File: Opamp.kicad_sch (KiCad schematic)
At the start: 7 parts, among them Q2 NPN, Q3 NPN, U1 ADA4522-2ARMZ-R7, U2 MCP4232-503E/UN

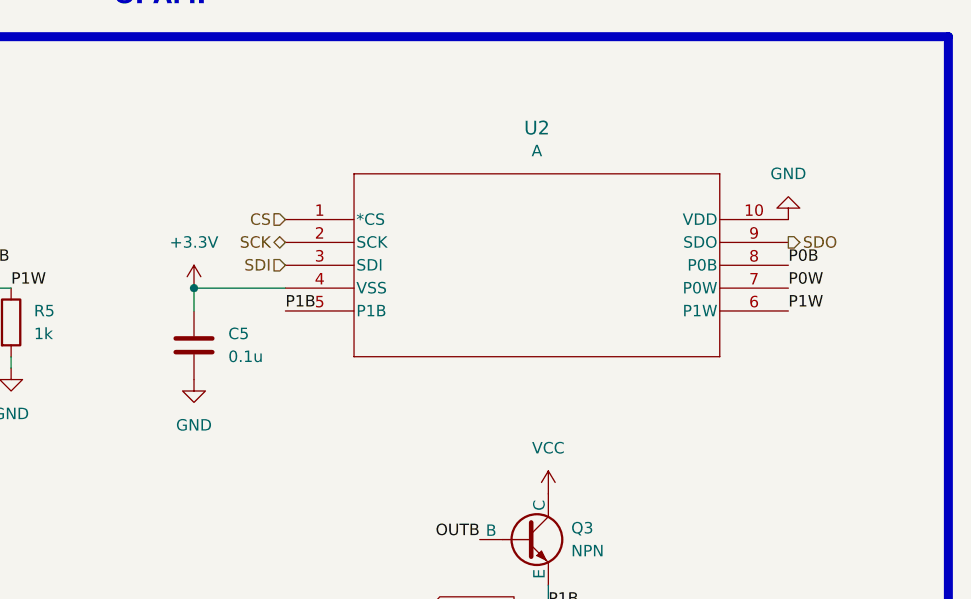
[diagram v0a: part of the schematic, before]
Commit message: version 2 with 0.8mm thickness
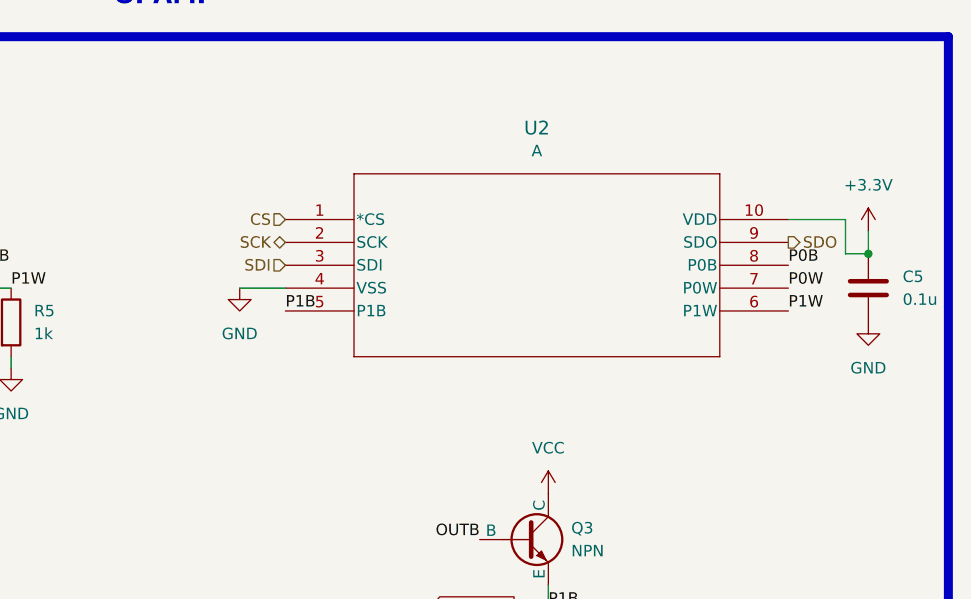
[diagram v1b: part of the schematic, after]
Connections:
- net +3.3V: now also U2.10 (VDD); no longer U2.4 (VSS)
- net GND: now also U2.4 (VSS); no longer U2.10 (VDD)
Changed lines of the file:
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@@
 (kicad_sch (version 20230121) (generator eeschema)
   (paper "A4")
-  (junction (at 152.4 88.9) (diameter 0) (color 0 0 0 0)
+  (junction (at 227.33 85.09) (diameter 0) (color 0 0 0 0)
   )
   (wire (pts (xy 187.96 124.46) (xy 191.77 124.46))
@@
     (stroke (width 0) (type default))
   )
-  (wire (pts (xy 152.4 88.9) (xy 162.56 88.9))
+  (wire (pts (xy 157.48 88.9) (xy 162.56 88.9))
+    (stroke (width 0) (type default))
+  )
+  (wire (pts (xy 224.79 81.28) (xy 224.79 85.09))
+    (stroke (width 0) (type default))
+  )
+  (wire (pts (xy 224.79 85.09) (xy 227.33 85.09))
+    (stroke (width 0) (type default))
+  )
+  (wire (pts (xy 227.33 85.09) (xy 227.33 82.55))
     (stroke (width 0) (type default))
   )
@@
     (stroke (width 0) (type default))
   )
-  (wire (pts (xy 152.4 91.44) (xy 152.4 88.9))
+  (wire (pts (xy 218.44 81.28) (xy 224.79 81.28))
     (stroke (width 0) (type default))
   )
@@
     (effects (font (size 1.27 1.27)) (justify right))
   )
-  (symbol (lib_id "Device:C") (at 152.4 95.25 0) (unit 1)
-    (in_bom yes) (on_board yes) (dnp no) (fields_autoplaced)
-    (property "Reference" "C5" (at 156.21 93.98 0)
-      (effects (font (size 1.27 1.27)) (justify left))
-    )
-    (property "Value" "0.1u" (at 156.21 96.52 0)
-      (effects (font (size 1.27 1.27)) (justify left))
-    )
-    (property "Footprint" "Capacitor_SMD:C_0402_1005Metric" (at 153.3652 99.06 0)
-      (effects (font (size 1.27 1.27)) hide)
-    )
-    (property "Datasheet" "~" (at 152.4 95.25 0)
-      (effects (font (size 1.27 1.27)) hide)
-    )
-    (property "Manufacturer" "Murata" (at 152.4 95.25 0)
-      (effects (font (size 1.27 1.27)) hide)
-    )
-    (property "Manufacturer Part Number" "GRM155R71H104KE14J" (at 152.4 95.25 0)
-      (effects (font (size 1.27 1.27)) hide)
-    )
-    (property "Package" "0402" (at 152.4 95.25 0)
-      (effects (font (size 1.27 1.27)) hide)
-    )
-    (property "Description" "CAP CER 0.1UF 50V X7R 0402" (at 152.4 95.25 0)
-      (effects (font (size 1.27 1.27)) hide)
-    )
-    (property "Long Description" "0.1 µF ±10% 50V Ceramic Capacitor X7R 0402 (1005 Metric)" (at 152.4 95.25 0)
-      (effects (font (size 1.27 1.27)) hide)
-    )
-    (property "Manufacturing Note" "D" (at 152.4 95.25 0)
-      (effects (font (size 1.27 1.27)) hide)
-    )
-    (pin "1")
-    (pin "2")
-    (instances
-      (project "MaxTENS"
-        (path "/19b6afc4-eb08-418e-8b76-b08e19c3eaa1/4e6d7f12-db51-4aea-bcff-0e7ea8ac0c76"
-          (reference "C5") (unit 1)
-        )
-      )
-    )
-  )
   (symbol (lib_id "power:GND") (at 72.39 93.98 0) (unit 1)
     (in_bom yes) (on_board yes) (dnp no) (fields_autoplaced)
@@
     )
   )
+  (symbol (lib_id "power:GND") (at 157.48 88.9 0) (unit 1)
+    (in_bom yes) (on_board yes) (dnp no) (fields_autoplaced)
+    (property "Reference" "#PWR013" (at 157.48 95.25 0)
+      (effects (font (size 1.27 1.27)) hide)
+    )
+    (property "Value" "GND" (at 157.48 93.98 0)
+      (effects (font (size 1.27 1.27)))
+    )
+    (property "Footprint" "" (at 157.48 88.9 0)
+      (effects (font (size 1.27 1.27)) hide)
+    )
+    (property "Datasheet" "" (at 157.48 88.9 0)
+      (effects (font (size 1.27 1.27)) hide)
+    )
+    (pin "1")
+    (instances
+      (project "MaxTENS"
+        (path "/19b6afc4-eb08-418e-8b76-b08e19c3eaa1/4e6d7f12-db51-4aea-bcff-0e7ea8ac0c76"
+          (reference "#PWR013") (unit 1)
+        )
+      )
+    )
+  )
   (symbol (lib_id "power:VCC") (at 123.19 83.82 0) (unit 1)
     (in_bom yes) (on_board yes) (dnp no) (fields_autoplaced)
@@
     )
   )
-  (symbol (lib_id "power:GND") (at 218.44 81.28 180) (unit 1)
-    (in_bom yes) (on_board yes) (dnp no) (fields_autoplaced)
-    (property "Reference" "#PWR013" (at 218.44 74.93 0)
-      (effects (font (size 1.27 1.27)) hide)
-    )
-    (property "Value" "GND" (at 218.44 76.2 0)
-      (effects (font (size 1.27 1.27)))
-    )
-    (property "Footprint" "" (at 218.44 81.28 0)
-      (effects (font (size 1.27 1.27)) hide)
-    )
-    (property "Datasheet" "" (at 218.44 81.28 0)
-      (effects (font (size 1.27 1.27)) hide)
-    )
-    (pin "1")
-    (instances
-      (project "MaxTENS"
-        (path "/19b6afc4-eb08-418e-8b76-b08e19c3eaa1/4e6d7f12-db51-4aea-bcff-0e7ea8ac0c76"
-          (reference "#PWR013") (unit 1)
-        )
-      )
-    )
-  )
   (symbol (lib_id "Device:R") (at 132.08 92.71 0) (unit 1)
     (in_bom yes) (on_board yes) (dnp no) (fields_autoplaced)
@@
     )
   )
-  (symbol (lib_id "power:GND") (at 152.4 99.06 0) (unit 1)
-    (in_bom yes) (on_board yes) (dnp no) (fields_autoplaced)
-    (property "Reference" "#PWR015" (at 152.4 105.41 0)
-      (effects (font (size 1.27 1.27)) hide)
-    )
-    (property "Value" "GND" (at 152.4 104.14 0)
-      (effects (font (size 1.27 1.27)))
-    )
-    (property "Footprint" "" (at 152.4 99.06 0)
-      (effects (font (size 1.27 1.27)) hide)
-    )
-    (property "Datasheet" "" (at 152.4 99.06 0)
+  (symbol (lib_id "power:GND") (at 227.33 92.71 0) (unit 1)
+    (in_bom yes) (on_board yes) (dnp no) (fields_autoplaced)
+    (property "Reference" "#PWR015" (at 227.33 99.06 0)
+      (effects (font (size 1.27 1.27)) hide)
+    )
+    (property "Value" "GND" (at 227.33 97.79 0)
+      (effects (font (size 1.27 1.27)))
+    )
+    (property "Footprint" "" (at 227.33 92.71 0)
+      (effects (font (size 1.27 1.27)) hide)
+    )
+    (property "Datasheet" "" (at 227.33 92.71 0)
       (effects (font (size 1.27 1.27)) hide)
     )
@@
         (path "/19b6afc4-eb08-418e-8b76-b08e19c3eaa1/4e6d7f12-db51-4aea-bcff-0e7ea8ac0c76"
           (reference "#PWR015") (unit 1)
+        )
+      )
+    )
+  )
+  (symbol (lib_id "power:+3.3V") (at 227.33 82.55 0) (unit 1)
+    (in_bom yes) (on_board yes) (dnp no) (fields_autoplaced)
+    (property "Reference" "#PWR012" (at 227.33 86.36 0)
+      (effects (font (size 1.27 1.27)) hide)
+    )
+    (property "Value" "+3.3V" (at 227.33 77.47 0)
+      (effects (font (size 1.27 1.27)))
+    )
+    (property "Footprint" "" (at 227.33 82.55 0)
+      (effects (font (size 1.27 1.27)) hide)
+    )
+    (property "Datasheet" "" (at 227.33 82.55 0)
+      (effects (font (size 1.27 1.27)) hide)
+    )
+    (pin "1")
+    (instances
+      (project "MaxTENS"
+        (path "/19b6afc4-eb08-418e-8b76-b08e19c3eaa1/4e6d7f12-db51-4aea-bcff-0e7ea8ac0c76"
+          (reference "#PWR012") (unit 1)
         )
       )
@@
     )
   )
-  (symbol (lib_id "power:+3.3V") (at 152.4 88.9 0) (unit 1)
-    (in_bom yes) (on_board yes) (dnp no) (fields_autoplaced)
-    (property "Reference" "#PWR012" (at 152.4 92.71 0)
-      (effects (font (size 1.27 1.27)) hide)
-    )
-    (property "Value" "+3.3V" (at 152.4 83.82 0)
-      (effects (font (size 1.27 1.27)))
-    )
-    (property "Footprint" "" (at 152.4 88.9 0)
-      (effects (font (size 1.27 1.27)) hide)
-    )
-    (property "Datasheet" "" (at 152.4 88.9 0)
-      (effects (font (size 1.27 1.27)) hide)
-    )
-    (pin "1")
-    (instances
-      (project "MaxTENS"
-        (path "/19b6afc4-eb08-418e-8b76-b08e19c3eaa1/4e6d7f12-db51-4aea-bcff-0e7ea8ac0c76"
-          (reference "#PWR012") (unit 1)
-        )
-      )
-    )
-  )
   (symbol (lib_id "power:VCC") (at 104.14 110.49 0) (unit 1)
     (in_bom yes) (on_board yes) (dnp no) (fields_autoplaced)
@@
         )
       )
+    )
+  )
+  (symbol (lib_id "Device:C") (at 227.33 88.9 0) (unit 1)
+    (in_bom yes) (on_board yes) (dnp no) (fields_autoplaced)
+    (property "Reference" "C5" (at 231.14 87.63 0)
+      (effects (font (size 1.27 1.27)) (justify left))
+    )
+    (property "Value" "0.1u" (at 231.14 90.17 0)
+      (effects (font (size 1.27 1.27)) (justify left))
+    )
+    (property "Footprint" "Capacitor_SMD:C_0402_1005Metric" (at 228.2952 92.71 0)
+      (effects (font (size 1.27 1.27)) hide)
+    )
+    (property "Datasheet" "~" (at 227.33 88.9 0)
+      (effects (font (size 1.27 1.27)) hide)
+    )
+    (property "Manufacturer" "Murata" (at 227.33 88.9 0)
+      (effects (font (size 1.27 1.27)) hide)
+    )
+    (property "Manufacturer Part Number" "GRM155R71H104KE14J" (at 227.33 88.9 0)
+      (effects (font (size 1.27 1.27)) hide)
+    )
+    (property "Package" "0402" (at 227.33 88.9 0)
+      (effects (font (size 1.27 1.27)) hide)
+    )
+    (property "Description" "CAP CER 0.1UF 50V X7R 0402" (at 227.33 88.9 0)
+      (effects (font (size 1.27 1.27)) hide)
+    )
+    (property "Long Description" "0.1 µF ±10% 50V Ceramic Capacitor X7R 0402 (1005 Metric)" (at 227.33 88.9 0)
+      (effects (font (size 1.27 1.27)) hide)
+    )
+    (property "Manufacturing Note" "D" (at 227.33 88.9 0)
+      (effects (font (size 1.27 1.27)) hide)
+    )
+    (pin "1")
+    (pin "2")
+    (instances
+      (project "MaxTENS"
+        (path "/19b6afc4-eb08-418e-8b76-b08e19c3eaa1/4e6d7f12-db51-4aea-bcff-0e7ea8ac0c76"
+          (reference "C5") (unit 1)
+        )
+      )

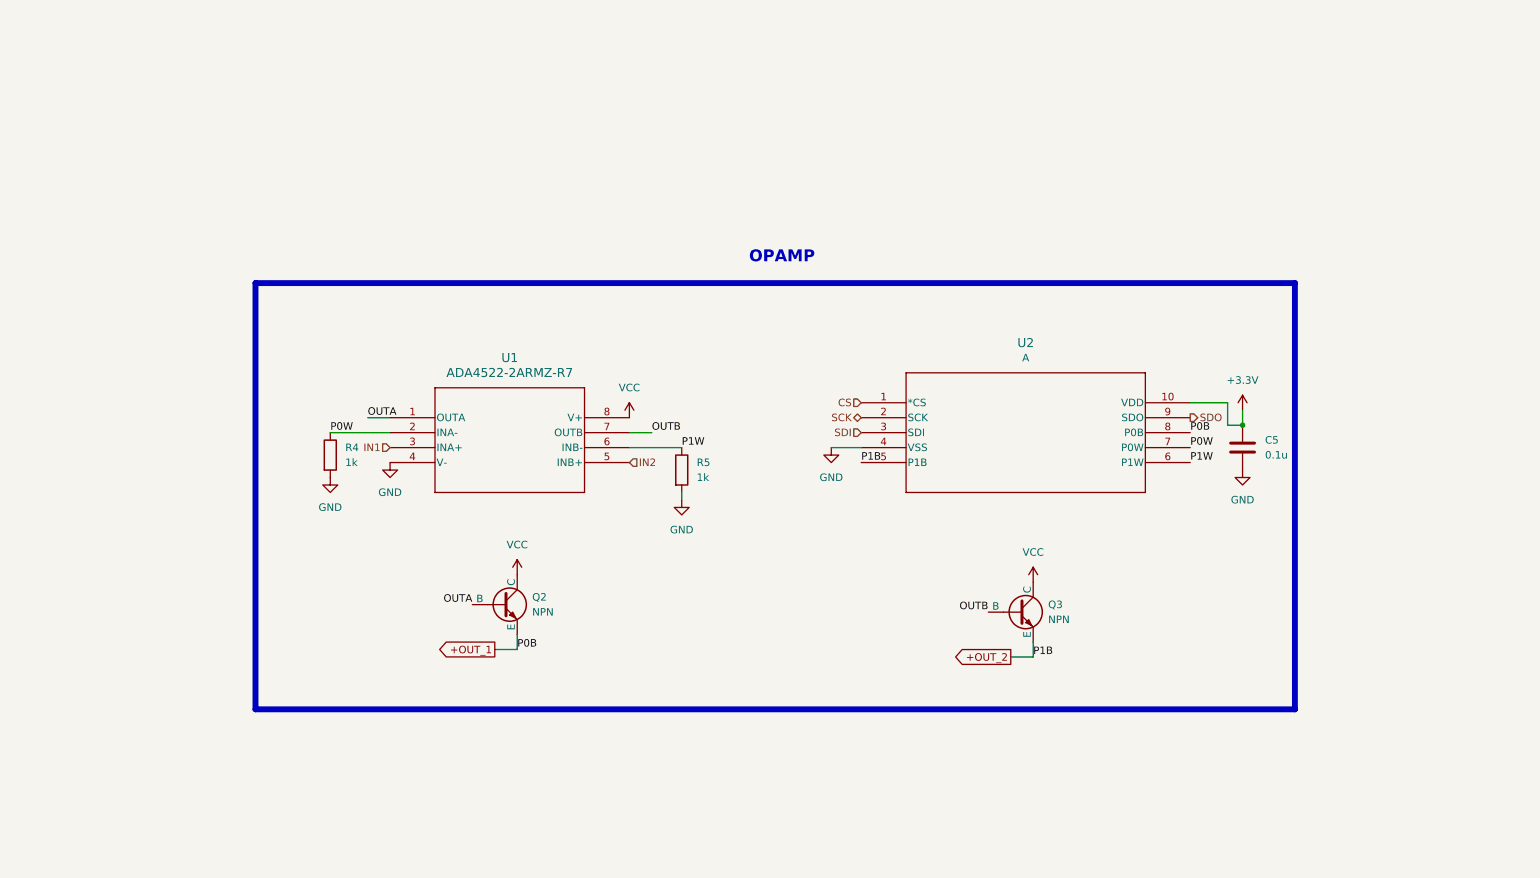
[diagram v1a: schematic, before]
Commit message: v3: removed digital potentiometer, added 8 discrete resistors and one GPIO expander
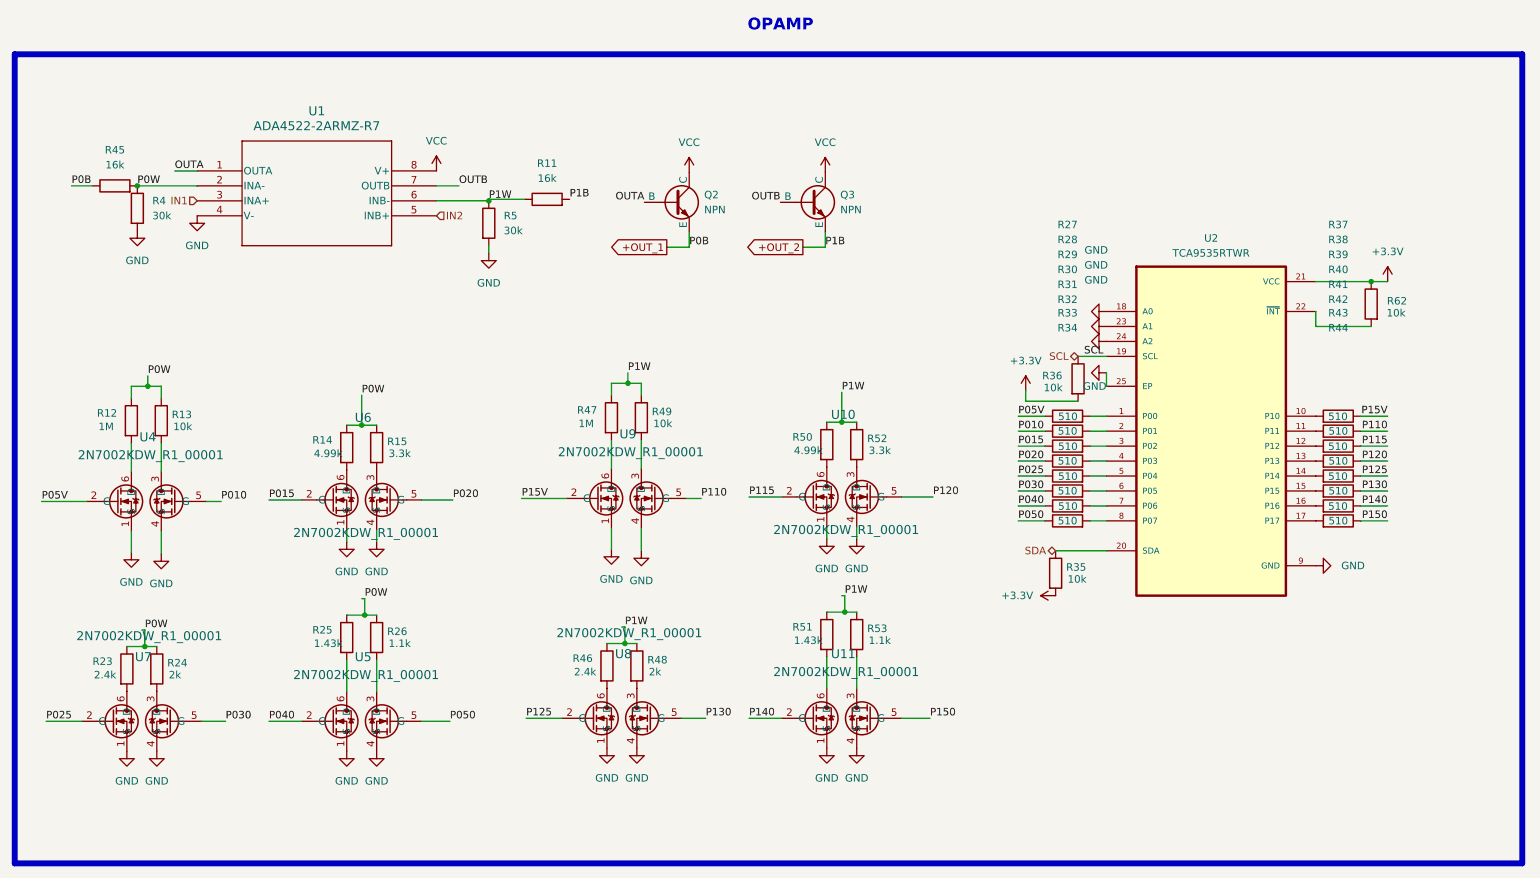
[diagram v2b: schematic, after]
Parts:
- removed C5: 0.1u, Capacitor_SMD:C_0402_1005Metric, symbol Device:C
- removed U2: MCP4232-503E/UN, Library:MSOP10_MC_MCH, symbol 2023-09-03_14-36-57:MCP4232-503E_UN
- added R11, R45: 16k, Resistor_SMD:R_0402_1005Metric, symbol Device:R
- added R12, R47: 1M, Resistor_SMD:R_0402_1005Metric, symbol Device:R
- added R13, R35, R36, R49, R62: 10k, Resistor_SMD:R_0402_1005Metric, symbol Device:R
- added R14, R50: 4.99k, Resistor_SMD:R_0402_1005Metric, symbol Device:R
- added R15, R52: 3.3k, Resistor_SMD:R_0402_1005Metric, symbol Device:R
- added R23, R46: 2.4k, Resistor_SMD:R_0402_1005Metric, symbol Device:R
- added R24, R48: 2k, Resistor_SMD:R_0402_1005Metric, symbol Device:R
- added R25, R51: 1.43k, Resistor_SMD:R_0402_1005Metric, symbol Device:R
- added R26, R53: 1.1k, Resistor_SMD:R_0402_1005Metric, symbol Device:R
- added R27, R28, R29, R30, R31, R32, R33, R34, R37, R38, R39, R40, R41, R42, R43, R44: 510, Resistor_SMD:R_0402_1005Metric, symbol Device:R
- added U10, U11, U4, U5, U6, U7, U8, U9: 2N7002KDW_R1_00001, SOT-363-6_2P2X1P35_ONS, symbol 2023-09-03_14-36-57:2N7002KDW_R1_00001
- added U2: TCA9535RTWR, Library:QFN50P400X400X80-25N, symbol 2023-09-03_14-36-57:TCA9535RTWR
- R4, R5: value 1k -> 30k; Long Description 1 kOhms ±1% 0.063W, 1/16W Chip Resistor 0402 (1005 Metric) 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 -> 30 kOhms ±0.1% 0.063W, 1/16W Chip Resistor 0402 (1005 Metri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; Manufacturer Part Number RC0402FR-101KL -> RT0402BRD0730KL
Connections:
- net +3.3V: now also R35.2, R36.2, R62.1, U2.21 (VCC)
- net +OUT_1: now also R45.1
- net +OUT_2: now also R11.2
- net GND: now also U10.1 (S), U10.4 (S), U11.1 (S), U11.4 (S), U2.18 (A0), U2.23 (A1), U2.24 (A2), U2.25 (EP), U2.9 (GND), U4.1 (S), U4.4 (S), U5.1 (S), U5.4 (S), U6.1 (S), U6.4 (S), U7.1 (S), U7.4 (S), U8.1 (S), U8.4 (S), U9.1 (S), U9.4 (S)
- net P0W: now also R12.1, R13.1, R14.1, R15.1, R23.1, R24.1, R25.1, R26.1, R45.2
- net P1W: now also R11.1, R46.1, R47.1, R48.1, R49.1, R50.1, R51.1, R52.1, R53.1
- new net: R41.2, U2.14 (P14)
- new net: R24.2, U7.3 (D)
- new net: R48.2, U8.3 (D)
- new net: R46.2, U8.6 (D)
- new net: R26.2, U5.3 (D)
- new net: R13.2, U4.3 (D)
- new net: R53.2, U11.3 (D)
- new net: R51.2, U11.6 (D)
- new net: R31.2, U2.5 (P04)
- new net: R50.2, U10.6 (D)
- new net: R30.2, U2.4 (P03)
- new net: R15.2, U6.3 (D)
- new net: R52.2, U10.3 (D)
- new net: R44.2, U2.17 (P17)
- new net: R23.2, U7.6 (D)
- new net: R49.2, U9.3 (D)
- new net: R47.2, U9.6 (D)
- new net: R25.2, U5.6 (D)
- new net: R37.2, U2.10 (P10)
- new net: R62.2, U2.22 (~{INT})
- new net: R27.2, U2.1 (P00)
- new net: R38.2, U2.11 (P11)
- new net: R39.2, U2.12 (P12)
- new net: R40.2, U2.13 (P13)
- new net: R42.2, U2.15 (P15)
- new net: R43.2, U2.16 (P16)
- new net: R28.2, U2.2 (P01)
- new net: R29.2, U2.3 (P02)
- new net: R32.2, U2.6 (P05)
- new net: R33.2, U2.7 (P06)
- new net: R34.2, U2.8 (P07)
- new net: R14.2, U6.6 (D)
- new net: R12.2, U4.6 (D)
- new net P010: R28.1, U4.5 (G)
- new net P015: R29.1, U6.2 (G)
- new net P020: R30.1, U6.5 (G)
- new net P025: R31.1, U7.2 (G)
- new net P030: R32.1, U7.5 (G)
- new net P040: R33.1, U5.2 (G)
- new net P050: R34.1, U5.5 (G)
- new net P05V: R27.1, U4.2 (G)
- new net P110: R38.1, U9.5 (G)
- new net P115: R39.1, U10.2 (G)
- new net P120: R40.1, U10.5 (G)
- new net P125: R41.1, U8.2 (G)
- new net P130: R42.1, U8.5 (G)
- new net P140: R43.1, U11.2 (G)
- new net P150: R44.1, U11.5 (G)
- new net P15V: R37.1, U9.2 (G)
- new net SCL: R36.1, U2.19 (SCL)
- new net SDA: R35.1, U2.20 (SDA)
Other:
- moved on the sheet: Q2, Q3, R5, U1
